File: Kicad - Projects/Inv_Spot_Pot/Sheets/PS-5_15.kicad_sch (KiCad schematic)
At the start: 29 parts, among them U2 LTV-817S

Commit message: Preparação para Manufatura
Validação de footprints

Serigrafia movida para melhorar legibilidade

Backup de versão com trafo anterior salvo

Adição de snippet de código para ativação da proteção térmica
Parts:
- CY3: footprint Capacitor_THT:C_Disc_D10.5mm_W5.0mm_P10.00mm -> Capacitor_THT:C_Disc_D10.5mm_W5.0mm_P7.50mm
- R12, R8: value 2k -> 2k2
- T3: footprint Transformer_THT:Transformer_Breve_TEZ-28x33 -> Custom_Transformer:EE25V-8T
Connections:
- net GND_{24V}: now also T3.3; no longer T3.4
- net ~{GND}: now also T3.6, T3.8; no longer T3.7, T3.9
- net at D4.2 (A): now also T3.4; no longer T3.5
- net at D6.2 (A): now also T3.5; no longer T3.6
- net at D5.2 (A): now also T3.7; no longer T3.8
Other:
- moved on the sheet: C14, C25, D25
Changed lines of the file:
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@@
 	)
 	(junction
-		(at 246.38 104.14)
+		(at 209.55 130.81)
 		(diameter 0)
 		(color 0 0 0 0)
 	)
 	(junction
-		(at 238.76 104.14)
+		(at 201.93 130.81)
 		(diameter 0)
 		(color 0 0 0 0)
@@
 	)
 	(junction
-		(at 238.76 115.57)
+		(at 201.93 142.24)
 		(diameter 0)
 		(color 0 0 0 0)
@@
 	(wire
 		(pts
-			(xy 226.06 104.14) (xy 228.6 104.14)
+			(xy 189.23 130.81) (xy 191.77 130.81)
 		)
 		(stroke
@@
 	(wire
 		(pts
-			(xy 238.76 104.14) (xy 238.76 105.41)
+			(xy 201.93 130.81) (xy 201.93 132.08)
 		)
 		(stroke
@@
 	(wire
 		(pts
-			(xy 246.38 113.03) (xy 246.38 115.57)
+			(xy 209.55 139.7) (xy 209.55 142.24)
 		)
 		(stroke
@@
 	(wire
 		(pts
-			(xy 238.76 104.14) (xy 246.38 104.14)
+			(xy 201.93 130.81) (xy 209.55 130.81)
 		)
 		(stroke
@@
 	(wire
 		(pts
-			(xy 236.22 104.14) (xy 238.76 104.14)
+			(xy 199.39 130.81) (xy 201.93 130.81)
 		)
 		(stroke
@@
 	(wire
 		(pts
-			(xy 226.06 115.57) (xy 238.76 115.57)
+			(xy 189.23 142.24) (xy 201.93 142.24)
 		)
 		(stroke
@@
 	(wire
 		(pts
-			(xy 238.76 115.57) (xy 238.76 113.03)
+			(xy 201.93 142.24) (xy 201.93 139.7)
 		)
 		(stroke
@@
 	(wire
 		(pts
-			(xy 246.38 104.14) (xy 250.19 104.14)
+			(xy 209.55 130.81) (xy 213.36 130.81)
 		)
 		(stroke
@@
 	(wire
 		(pts
-			(xy 246.38 104.14) (xy 246.38 105.41)
+			(xy 209.55 130.81) (xy 209.55 132.08)
 		)
 		(stroke
@@
 	(wire
 		(pts
-			(xy 246.38 115.57) (xy 238.76 115.57)
+			(xy 209.55 142.24) (xy 201.93 142.24)
 		)
 		(stroke
@@
 	(hierarchical_label "GND_{24V}"
 		(shape input)
-		(at 226.06 115.57 180)
+		(at 189.23 142.24 180)
 		(effects
 			(font
@@
 	(hierarchical_label "24V"
 		(shape input)
-		(at 226.06 104.14 180)
+		(at 189.23 130.81 180)
 		(effects
 			(font
@@
 	(hierarchical_label "24V-Cooler"
 		(shape input)
-		(at 250.19 104.14 0)
+		(at 213.36 130.81 0)
 		(effects
 			(font
@@
 			)
 		)
-		(property "Value" "2k"
+		(property "Value" "2k2"
 			(at 109.22 60.9599 0)
-			(hide yes)
 			(show_name no)
 			(do_not_autoplace no)
@@
 	(symbol
 		(lib_id "Device:C_Polarized")
-		(at 238.76 109.22 0)
+		(at 201.93 135.89 0)
 		(unit 1)
 		(body_style 1)
@@
 		(dnp no)
 		(property "Reference" "C14"
-			(at 236.982 107.188 0)
+			(at 200.152 133.858 0)
 			(show_name no)
 			(do_not_autoplace no)
@@
 		)
 		(property "Value" "47u"
-			(at 237.236 111.506 0)
+			(at 200.406 138.176 0)
 			(show_name no)
 			(do_not_autoplace no)
@@
 		)
 		(property "Footprint" "Capacitor_THT:CP_Radial_D6.3mm_P2.50mm"
-			(at 239.7252 113.03 0)
+			(at 202.8952 139.7 0)
 			(hide yes)
 			(show_name no)
@@
 		)
 		(property "Datasheet" ""
-			(at 238.76 109.22 0)
+			(at 201.93 135.89 0)
 			(hide yes)
 			(show_name no)
@@
 		)
 		(property "Description" "Polarized capacitor"
-			(at 238.76 109.22 0)
+			(at 201.93 135.89 0)
 			(hide yes)
 			(show_name no)
@@
 			)
 		)
-		(property "Footprint" "Capacitor_THT:C_Disc_D10.5mm_W5.0mm_P10.00mm"
+		(property "Footprint" "Capacitor_THT:C_Disc_D10.5mm_W5.0mm_P7.50mm"
 			(at 193.3448 110.49 0)
 			(hide yes)
@@
 			)
 		)
-		(property "Footprint" "Transformer_THT:Transformer_Breve_TEZ-28x33"
+		(property "Footprint" "Custom_Transformer:EE25V-8T"
 			(at 133.35 68.58 0)
 			(hide yes)
@@
 		(pin "6"
 		)
-		(pin "9"
+		(pin "3"
 		)
 		(instances
@@
 			)
 		)
-		(property "Value" "2k"
+		(property "Value" "2k2"
 			(at 162.56 128.2699 0)
 			(show_name no)
@@
 	(symbol
 		(lib_id "Device:C")
-		(at 246.38 109.22 0)
+		(at 209.55 135.89 0)
 		(unit 1)
 		(body_style 1)
@@
 		(fields_autoplaced yes)
 		(property "Reference" "C25"
-			(at 250.19 107.9499 0)
+			(at 213.36 134.6199 0)
 			(show_name no)
 			(do_not_autoplace no)
@@
 		)
 		(property "Value" "100n"
-			(at 250.19 110.4899 0)
+			(at 213.36 137.1599 0)
 			(show_name no)
 			(do_not_autoplace no)
@@
 		)
 		(property "Footprint" "Capacitor_SMD:C_1206_3216Metric_Pad1.33x1.80mm_HandSolder"
-			(at 247.3452 113.03 0)
+			(at 210.5152 139.7 0)
 			(hide yes)
 			(show_name no)
@@
 		)
 		(property "Datasheet" ""
-			(at 246.38 109.22 0)
+			(at 209.55 135.89 0)
 			(hide yes)
 			(show_name no)
@@
 		)
 		(property "Description" "Unpolarized capacitor"
-			(at 246.38 109.22 0)
+			(at 209.55 135.89 0)
 			(hide yes)
 			(show_name no)
@@
 	(symbol
 		(lib_id "Device:D")
-		(at 232.41 104.14 0)
+		(at 195.58 130.81 0)
 		(mirror y)
 		(unit 1)
@@
 		(fields_autoplaced yes)
 		(property "Reference" "D25"
-			(at 232.41 97.79 0)
+			(at 195.58 124.46 0)
 			(show_name no)
 			(do_not_autoplace no)
@@
 		)
 		(property "Value" "M7"
-			(at 232.41 100.33 0)
+			(at 195.58 127 0)
 			(show_name no)
 			(do_not_autoplace no)
@@
 		)
 		(property "Footprint" "Diode_SMD:D_SMA"
-			(at 232.41 104.14 0)
+			(at 195.58 130.81 0)
 			(hide yes)
 			(show_name no)
@@
 		)
 		(property "Datasheet" ""
-			(at 232.41 104.14 0)
+			(at 195.58 130.81 0)
 			(hide yes)
 			(show_name no)
@@
 		)
 		(property "Description" "Diode"
-			(at 232.41 104.14 0)
+			(at 195.58 130.81 0)
 			(hide yes)
 			(show_name no)
@@
 		)
 		(property "Sim.Device" "D"
-			(at 232.41 104.14 0)
+			(at 195.58 130.81 0)
 			(hide yes)
 			(show_name no)
@@
 		)
 		(property "Sim.Pins" "1=K 2=A"
-			(at 232.41 104.14 0)
+			(at 195.58 130.81 0)
 			(hide yes)
 			(show_name no)

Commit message: Toques Finais
Ajustes finais antes da produção
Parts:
- CY3: footprint Capacitor_THT:C_Disc_D10.5mm_W5.0mm_P7.50mm -> Custom_Capacitors:C_Disc_D7.0mm_W2.5mm_P7.50mm
- D7: value BZV55B15 -> BZV55B12
- R7: value 510 -> 2k7
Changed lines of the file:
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@@
 	)
 	(junction
+		(at 115.57 41.91)
+		(diameter 0)
+		(color 0 0 0 0)
+	)
+	(junction
 		(at 69.85 102.87)
 		(diameter 0)
@@
 	(wire
 		(pts
+			(xy 115.57 40.64) (xy 115.57 41.91)
+		)
+		(stroke
+			(width 0)
+			(type default)
+		)
+	)
+	(wire
+		(pts
 			(xy 90.17 54.61) (xy 78.74 54.61)
 		)
@@
 		)
 	)
+	(netclass_flag ""
+		(length 2.54)
+		(shape round)
+		(at 115.57 40.64 0)
+		(fields_autoplaced yes)
+		(effects
+			(font
+				(size 1.27 1.27)
+			)
+			(justify left bottom)
+		)
+		(property "Classes da rede" "HVLC"
+			(at 116.2685 38.1 0)
+			(show_name no)
+			(do_not_autoplace no)
+			(effects
+				(font
+					(size 1.27 1.27)
+				)
+				(justify left)
+			)
+		)
+		(property "Component Class" ""
+			(at -31.75 -27.94 0)
+			(show_name no)
+			(do_not_autoplace no)
+			(effects
+				(font
+					(size 1.27 1.27)
+					(italic yes)
+				)
+			)
+		)
+	)
 	(symbol
 		(lib_id "Device:C_Polarized")
@@
 			)
 		)
-		(property "Value" "BZV55B15"
+		(property "Value" "BZV55B12"
 			(at 154.94 116.8399 90)
 			(show_name no)
@@
 			)
 		)
-		(property "Footprint" "Capacitor_THT:C_Disc_D10.5mm_W5.0mm_P7.50mm"
+		(property "Footprint" "Custom_Capacitors:C_Disc_D7.0mm_W2.5mm_P7.50mm"
 			(at 193.3448 110.49 0)
 			(hide yes)
@@
 			)
 		)
-		(property "Value" "510"
+		(property "Value" "2k7"
 			(at 160.02 106.6799 0)
 			(show_name no)

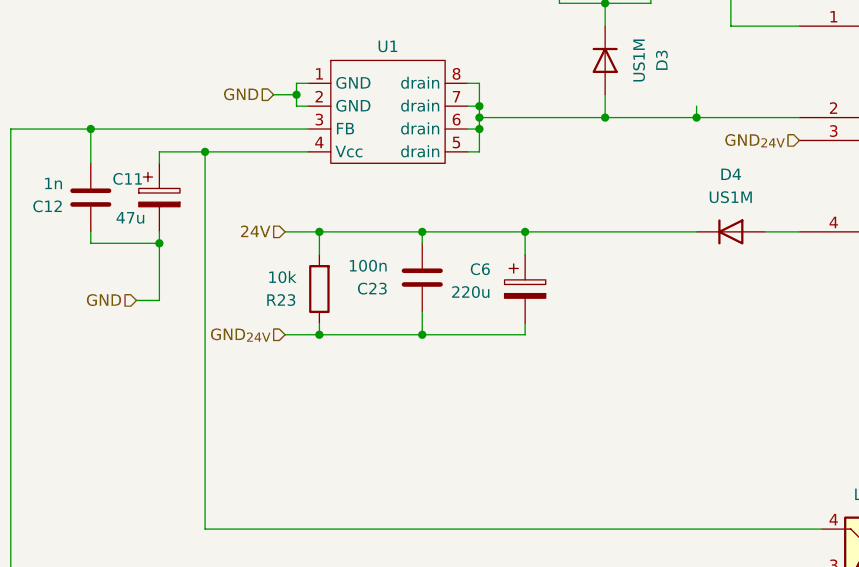
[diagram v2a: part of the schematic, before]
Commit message: Finalização - Placa Protótipo
Versão final da placa protótipo - placa já validada

Alterações:
 - Melhoras no plano terra para retorno de potência
 - Blindagem das trilhas de PWM para os IGBTs inferiores
 - Alargamento das trilhas de saída para a retificação

Falta:
 - Colocar todos os SMDs no lado TOP da placa
 - Ajustar posição dos IGBTs e transformador
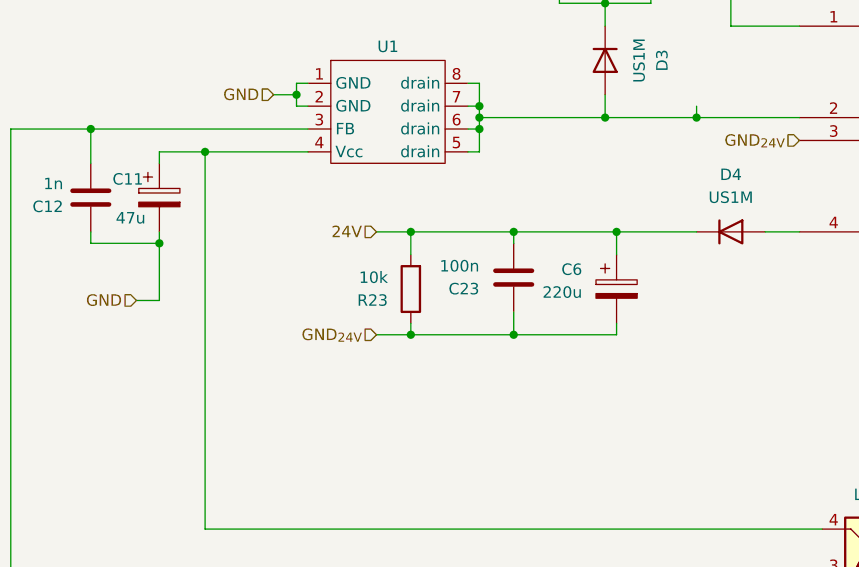
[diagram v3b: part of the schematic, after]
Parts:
- C13: Partnumber (none) -> CK45-B3DD472KYVNA
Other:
- moved on the sheet: C23, C6, R23
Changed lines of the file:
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@@
 	)
 	(junction
-		(at 69.85 91.44)
+		(at 80.01 91.44)
 		(diameter 0)
 		(color 0 0 0 0)
@@
 	)
 	(junction
-		(at 69.85 102.87)
+		(at 80.01 102.87)
 		(diameter 0)
 		(color 0 0 0 0)
@@
 	)
 	(junction
-		(at 81.28 102.87)
+		(at 91.44 102.87)
 		(diameter 0)
 		(color 0 0 0 0)
@@
 	)
 	(junction
-		(at 81.28 91.44)
+		(at 91.44 91.44)
 		(diameter 0)
 		(color 0 0 0 0)
@@
 	)
 	(junction
-		(at 92.71 91.44)
+		(at 102.87 91.44)
 		(diameter 0)
 		(color 0 0 0 0)
@@
 	(wire
 		(pts
-			(xy 81.28 100.33) (xy 81.28 102.87)
+			(xy 91.44 100.33) (xy 91.44 102.87)
 		)
 		(stroke
@@
 	(wire
 		(pts
-			(xy 81.28 92.71) (xy 81.28 91.44)
+			(xy 91.44 92.71) (xy 91.44 91.44)
 		)
 		(stroke
@@
 	(wire
 		(pts
-			(xy 81.28 102.87) (xy 69.85 102.87)
+			(xy 91.44 102.87) (xy 80.01 102.87)
 		)
 		(stroke
@@
 	(wire
 		(pts
-			(xy 92.71 102.87) (xy 92.71 101.6)
+			(xy 102.87 102.87) (xy 102.87 101.6)
 		)
 		(stroke
@@
 	(wire
 		(pts
-			(xy 69.85 93.98) (xy 69.85 91.44)
+			(xy 80.01 93.98) (xy 80.01 91.44)
 		)
 		(stroke
@@
 	(wire
 		(pts
-			(xy 111.76 91.44) (xy 92.71 91.44)
+			(xy 111.76 91.44) (xy 102.87 91.44)
 		)
 		(stroke
@@
 	(wire
 		(pts
-			(xy 81.28 102.87) (xy 92.71 102.87)
+			(xy 91.44 102.87) (xy 102.87 102.87)
 		)
 		(stroke
@@
 	(wire
 		(pts
-			(xy 69.85 102.87) (xy 66.04 102.87)
+			(xy 80.01 102.87) (xy 76.2 102.87)
 		)
 		(stroke
@@
 	(wire
 		(pts
-			(xy 69.85 91.44) (xy 66.04 91.44)
+			(xy 80.01 91.44) (xy 76.2 91.44)
 		)
 		(stroke
@@
 	(wire
 		(pts
-			(xy 92.71 91.44) (xy 92.71 93.98)
+			(xy 102.87 91.44) (xy 102.87 93.98)
 		)
 		(stroke
@@
 	(wire
 		(pts
-			(xy 92.71 91.44) (xy 81.28 91.44)
+			(xy 102.87 91.44) (xy 91.44 91.44)
 		)
 		(stroke
@@
 	(wire
 		(pts
-			(xy 69.85 101.6) (xy 69.85 102.87)
+			(xy 80.01 101.6) (xy 80.01 102.87)
 		)
 		(stroke
@@
 	(wire
 		(pts
-			(xy 81.28 91.44) (xy 69.85 91.44)
+			(xy 91.44 91.44) (xy 80.01 91.44)
 		)
 		(stroke
@@
 	(hierarchical_label "24V"
 		(shape input)
-		(at 66.04 91.44 180)
+		(at 76.2 91.44 180)
 		(effects
 			(font
@@
 	(hierarchical_label "GND_{24V}"
 		(shape input)
-		(at 66.04 102.87 180)
+		(at 76.2 102.87 180)
 		(effects
 			(font
@@
 	(symbol
 		(lib_id "Device:C_Polarized")
-		(at 92.71 97.79 0)
+		(at 102.87 97.79 0)
 		(unit 1)
 		(body_style 1)
@@
 		(dnp no)
 		(property "Reference" "C6"
-			(at 88.9 95.6309 0)
+			(at 99.06 95.6309 0)
 			(show_name no)
 			(do_not_autoplace no)
@@
 		)
 		(property "Value" "220u"
-			(at 88.9 98.1709 0)
+			(at 99.06 98.1709 0)
 			(show_name no)
 			(do_not_autoplace no)
@@
 		)
 		(property "Footprint" "Capacitor_THT:CP_Radial_D8.0mm_P3.50mm"
-			(at 93.6752 101.6 0)
+			(at 103.8352 101.6 0)
 			(hide yes)
 			(show_name no)
@@
 		)
 		(property "Datasheet" ""
-			(at 92.71 97.79 0)
+			(at 102.87 97.79 0)
 			(hide yes)
 			(show_name no)
@@
 		)
 		(property "Description" "Polarized capacitor"
-			(at 92.71 97.79 0)
+			(at 102.87 97.79 0)
 			(hide yes)
 			(show_name no)
@@
 			)
 		)
+		(property "Partnumber" "CK45-B3DD472KYVNA"
+			(at 96.52 59.69 0)
+			(hide yes)
+			(show_name no)
+			(do_not_autoplace no)
+			(effects
+				(font
+					(size 1.27 1.27)
+				)
+			)
+		)
 		(pin "2"
 		)
@@
 	(symbol
 		(lib_id "Device:R")
-		(at 69.85 97.79 180)
+		(at 80.01 97.79 180)
 		(unit 1)
 		(body_style 1)
@@
 		(fields_autoplaced yes)
 		(property "Reference" "R23"
-			(at 67.31 99.0601 0)
+			(at 77.47 99.0601 0)
 			(show_name no)
 			(do_not_autoplace no)
@@
 		)
 		(property "Value" "10k"
-			(at 67.31 96.5201 0)
+			(at 77.47 96.5201 0)
 			(show_name no)
 			(do_not_autoplace no)
@@
 		)
 		(property "Footprint" "Resistor_SMD:R_1206_3216Metric_Pad1.30x1.75mm_HandSolder"
-			(at 71.628 97.79 90)
+			(at 81.788 97.79 90)
 			(hide yes)
 			(show_name no)
@@
 		)
 		(property "Datasheet" ""
-			(at 69.85 97.79 0)
+			(at 80.01 97.79 0)
 			(hide yes)
 			(show_name no)
@@
 		)
 		(property "Description" "Resistor"
-			(at 69.85 97.79 0)
+			(at 80.01 97.79 0)
 			(hide yes)
 			(show_name no)
@@
 	(symbol
 		(lib_id "Device:C")
-		(at 81.28 96.52 180)
+		(at 91.44 96.52 180)
 		(unit 1)
 		(body_style 1)
@@
 		(fields_autoplaced yes)
 		(property "Reference" "C23"
-			(at 77.47 97.7901 0)
+			(at 87.63 97.7901 0)
 			(show_name no)
 			(do_not_autoplace no)
@@
 		)
 		(property "Value" "100n"
-			(at 77.47 95.2501 0)
+			(at 87.63 95.2501 0)
 			(show_name no)
 			(do_not_autoplace no)
@@
 		)
 		(property "Footprint" "Capacitor_SMD:C_1206_3216Metric_Pad1.33x1.80mm_HandSolder"
-			(at 80.3148 92.71 0)
+			(at 90.4748 92.71 0)
 			(hide yes)
 			(show_name no)
@@
 		)
 		(property "Datasheet" ""
-			(at 81.28 96.52 0)
+			(at 91.44 96.52 0)
 			(hide yes)
 			(show_name no)
@@
 		)
 		(property "Description" "Unpolarized capacitor"
-			(at 81.28 96.52 0)
+			(at 91.44 96.52 0)
 			(hide yes)
 			(show_name no)

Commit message: Atualização de Footprints
Atualização de footprints dos transformadores principal e da fonte auxiliar
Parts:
- T3: footprint Custom_Transformer:EE25V-8T -> Transformer_THT:Transformer_Breve_TEZ-28x33
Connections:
- net GND_{24V}: now also T3.4; no longer T3.3
- net ~{GND}: now also T3.7, T3.9; no longer T3.6, T3.8
- net at D4.2 (A): now also T3.5; no longer T3.4
- net at D6.2 (A): now also T3.6; no longer T3.5
- net at D5.2 (A): now also T3.10; no longer T3.7
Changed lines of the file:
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@@
 			)
 		)
-		(property "Footprint" "Custom_Transformer:EE25V-8T"
+		(property "Footprint" "Transformer_THT:Transformer_Breve_TEZ-28x33"
 			(at 133.35 68.58 0)
 			(hide yes)
@@
 		(pin "5"
 		)
-		(pin "8"
+		(pin "10"
 		)
 		(pin "1"
@@
 		(pin "6"
 		)
-		(pin "3"
+		(pin "9"
 		)
 		(instances

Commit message: SMD no TOP
Todos SMDs transferidos para camada TOP
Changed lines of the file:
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@@
-	)
-	(junction
-		(at 115.57 41.91)
-		(diameter 0)
-		(color 0 0 0 0)
 	)
 	(junction
@@
 		(pts
 			(xy 35.56 80.01) (xy 35.56 129.54)
-		)
-		(stroke
-			(width 0)
-			(type default)
-		)
-	)
-	(wire
-		(pts
-			(xy 115.57 40.64) (xy 115.57 41.91)
 		)
 		(stroke
@@
 			(show_name no)
 			(do_not_autoplace no)
-			(effects
-				(font
-					(size 1.27 1.27)
-					(italic yes)
-				)
-			)
-		)
-	)
-	(netclass_flag ""
-		(length 2.54)
-		(shape round)
-		(at 115.57 40.64 0)
-		(fields_autoplaced yes)
-		(effects
-			(font
-				(size 1.27 1.27)
-			)
-			(justify left bottom)
-		)
-		(property "Classes da rede" "HVLC"
-			(at 116.2685 38.1 0)
-			(show_name no)
-			(do_not_autoplace no)
-			(effects
-				(font
-					(size 1.27 1.27)
-				)
-				(justify left)
-			)
-		)
-		(property "Component Class" ""
-			(at -31.75 -27.94 0)
-			(show_name no)
-			(do_not_autoplace no)
